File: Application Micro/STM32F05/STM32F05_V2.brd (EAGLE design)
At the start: 100 x 80 mm, 46 parts, among them T1 FDN340P, T2 AP1117_LIN_REG

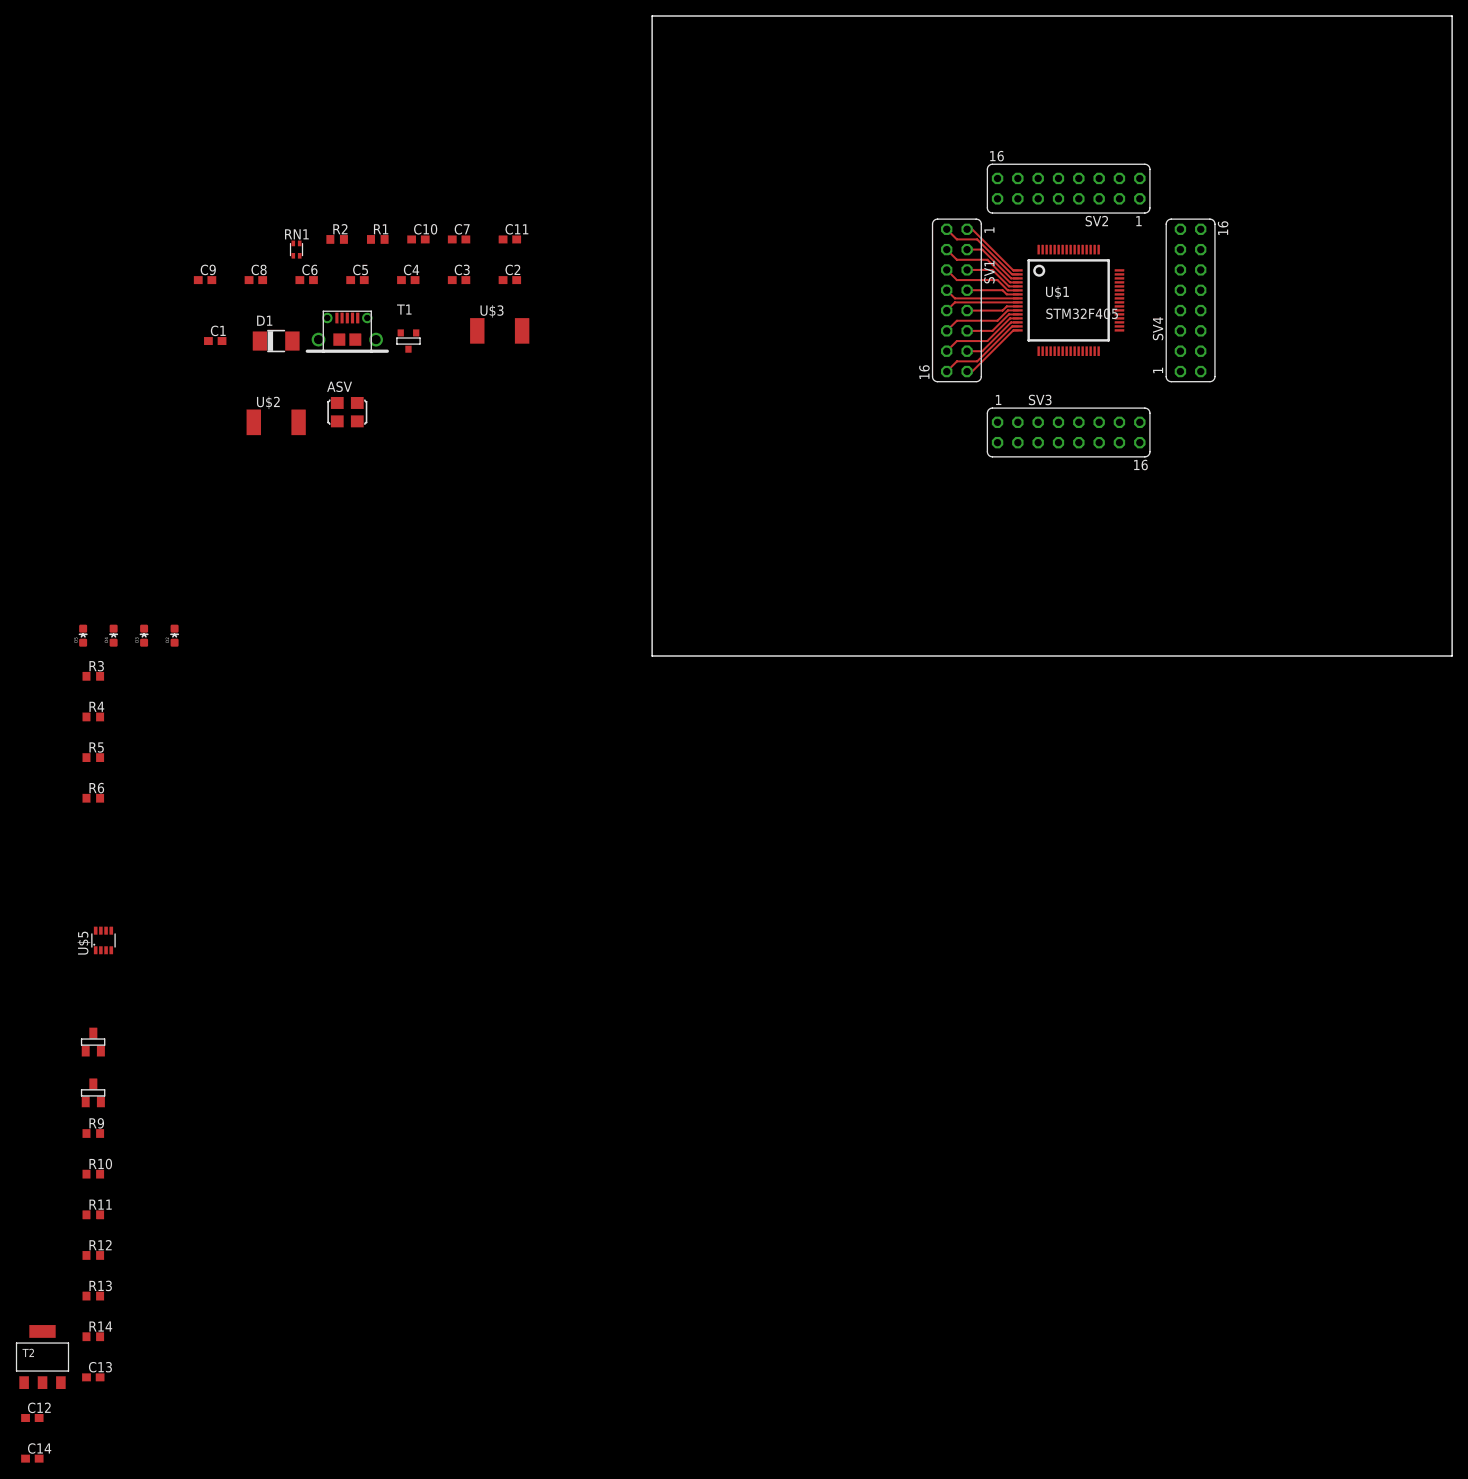
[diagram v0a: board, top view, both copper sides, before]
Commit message: Application Micro V2
Removed shift regulator (for I2C), named pins, connected can circuit to
can schematic.
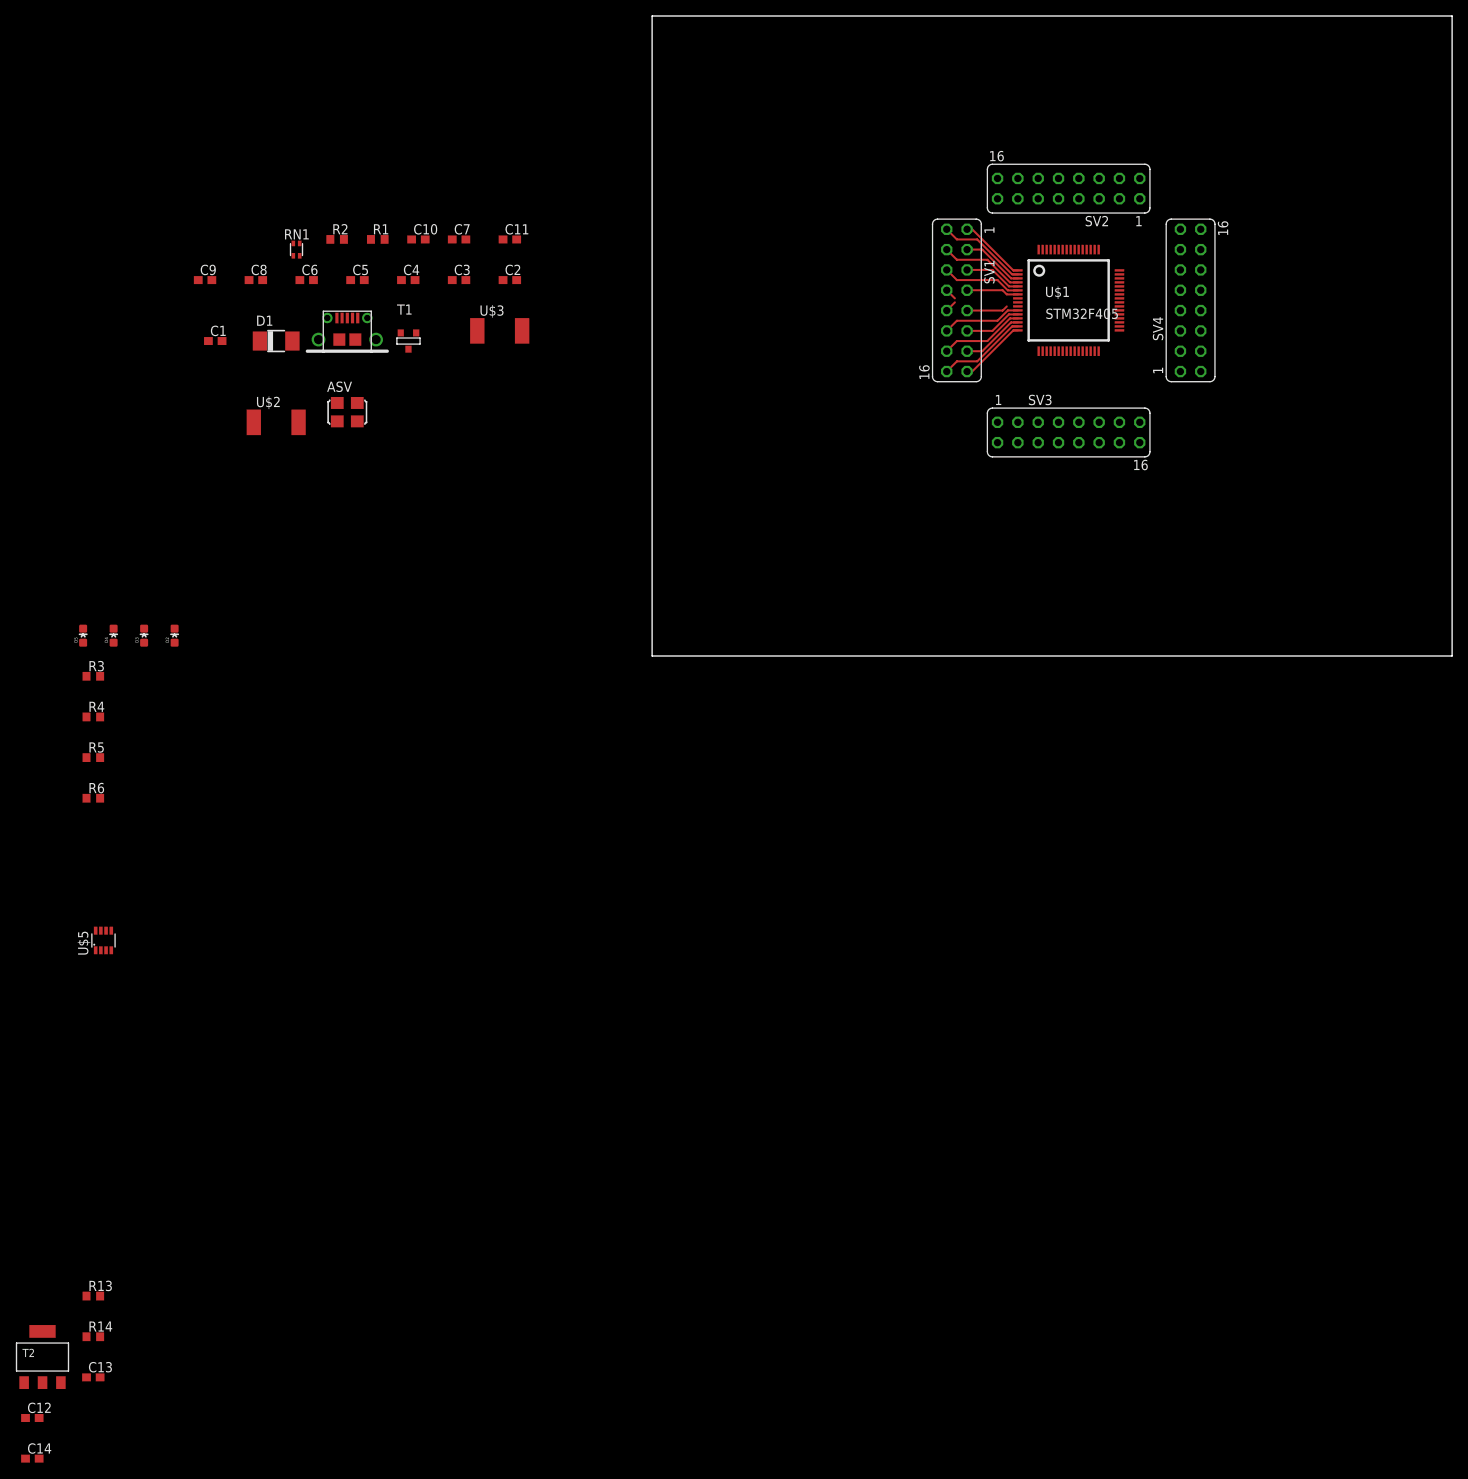
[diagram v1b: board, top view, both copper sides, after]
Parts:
- removed BSS138: n-chanel mosfet, DiscreteComponents:SOT-23-BSS138
- removed R10, R11, R12, R9: 10K, rcl:R0603
- removed U$6: BSS138, DiscreteComponents:SOT-23-BSS138
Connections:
- net PIN22 renamed CAM_LED
- net PIN58 renamed TEMP_SENS
- net PIN8 renamed SHFT_REG_DATA
- removed net PIN10: SV1.9, U$1.10
- removed net PIN33: SV4.1, U$1.33
- removed net PIN34: SV4.2, U$1.34
- removed net PIN37: SV4.5, U$1.37
- removed net PIN38: SV4.6, U$1.38
- removed net PIN39: SV4.7, U$1.39
- removed net PIN40: SV4.8, U$1.40
- removed net PIN44: SV4.12, U$1.44
- removed net PIN9: SV1.10, U$1.9
- removed net RXD: U$5.4
- removed net SCL1: BSS138.3, R11.1
- removed net SCL2: BSS138.2, R9.1
- removed net SDA1: R12.1, U$6.3
- removed net SDA2: R10.1, U$6.2
- removed net TXD: U$5.1
- new net CAN2_RX: SV4.1, U$1.33, U$5.4
- new net CAN2_TX: SV4.2, U$1.34, U$5.1
- new net DBUG_LED1: R3.2, SV4.8, U$1.40
- new net DBUG_LED2: R4.2, SV4.7, U$1.39
- new net DBUG_LED3: R5.2, SV4.6, U$1.38
- new net DBUG_LED4: R6.2, SV4.5, U$1.37
- new net SHFT_REG_CLK: SV1.9, U$1.9
- new net SHFT_REG_EN: SV1.10, U$1.10
- net +3V3: no longer BSS138.1, R11.2, R12.2, U$6.1
- net +5V: no longer R10.2, R9.2
- net PIN43: no longer SV4.11
- net PIN45: no longer U$1.45
- net USBD+: now also SV4.12, U$1.45
- net USBD-: now also SV4.11, U$1.44
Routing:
- net PIN9: track 9.31 -> 0.00 mm
- net SHFT_REG_DATA: track 9.31 -> 1.44 mm
- net PIN10: track 6.57 -> 0.00 mm
- net SHFT_REG_CLK: track 0.00 -> 5.18 mm
- net SHFT_REG_EN: track 0.00 -> 1.44 mm

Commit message: Started Routing
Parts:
- R3, R4, R6: value 10K -> 82
- R5: value 10K -> 10
- moved R14 190.2 mm to (76.7, 36.1), turned to 180 degrees
- moved R13 188.4 mm to (76.7, 38.4), turned to 180 degrees
- moved C12 187.8 mm to (68.3, 23.1), turned to 270 degrees
- moved C14 187.4 mm to (63.5, 23.1), turned to 90 degrees
- moved T2 184.1 mm to (66.0, 29.2)
- moved C13 176.9 mm to (66.0, 23.1), turned to 90 degrees
- moved U$5 165.0 mm to (76.7, 42.7), turned to 180 degrees
- moved R6 151.0 mm to (70.4, 38.4), turned to 180 degrees
- moved R5 150.0 mm to (70.4, 40.6), turned to 180 degrees
- moved R4 149.0 mm to (70.4, 42.9), turned to 180 degrees
- moved D5 148.9 mm to (73.4, 38.4), turned to 270 degrees
- moved R3 148.1 mm to (70.4, 45.2), turned to 180 degrees
- moved D4 145.8 mm to (73.4, 40.6), turned to 270 degrees
- moved D3 142.7 mm to (73.4, 42.9), turned to 270 degrees
- moved D2 139.8 mm to (73.4, 45.2), turned to 270 degrees
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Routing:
- net +3V3: track 19.1 -> 96.5 mm, vias 0 -> 1
- net GND: track 7.20 -> 46.7 mm, vias 0 -> 4
- net CAN2_RX: track 0.00 -> 28.2 mm, vias 0 -> 2
- net BOOT0: track 0.00 -> 24.5 mm
- net NRST: track 6.57 -> 24.4 mm
- net DBUG_LED4: track 0.00 -> 12.9 mm
- net DBUG_LED1: track 0.00 -> 12.4 mm
- net DBUG_LED2: track 0.00 -> 12.3 mm
- net DBUG_LED3: track 0.00 -> 12.1 mm
- net USBD+: track 0.00 -> 12.1 mm
- net USBD-: track 0.00 -> 11.8 mm
- net PIN62: track 0.00 -> 11.3 mm
- net PIN30: track 0.00 -> 11.3 mm
- net PIN50: track 0.00 -> 10.6 mm
- net CAN2_TX: track 0.00 -> 10.6 mm
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- added copper zone on layer 1, net GND
- added copper zone on layer 16, net GND
